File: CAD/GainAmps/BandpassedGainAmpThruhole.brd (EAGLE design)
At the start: 7.4 x 22.4 mm, 9 parts, among them U1 OPA202IDGKR

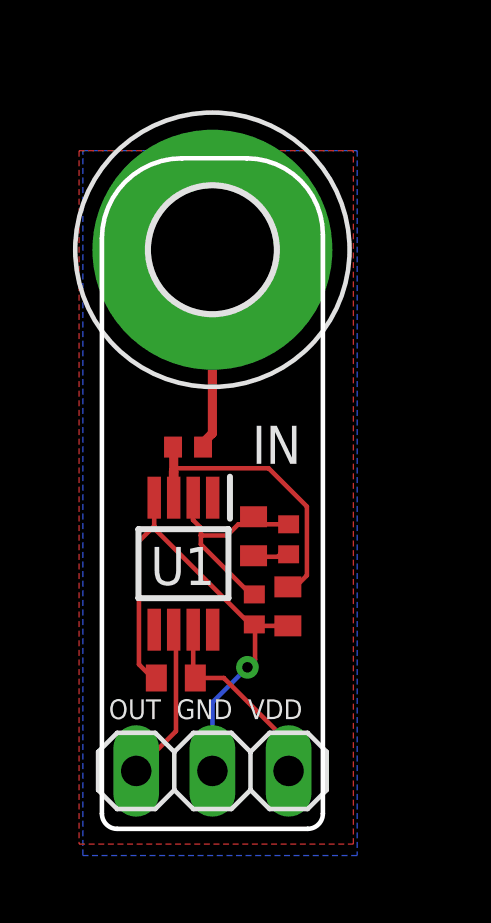
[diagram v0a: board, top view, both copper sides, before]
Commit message: moved, added production files for gain amps
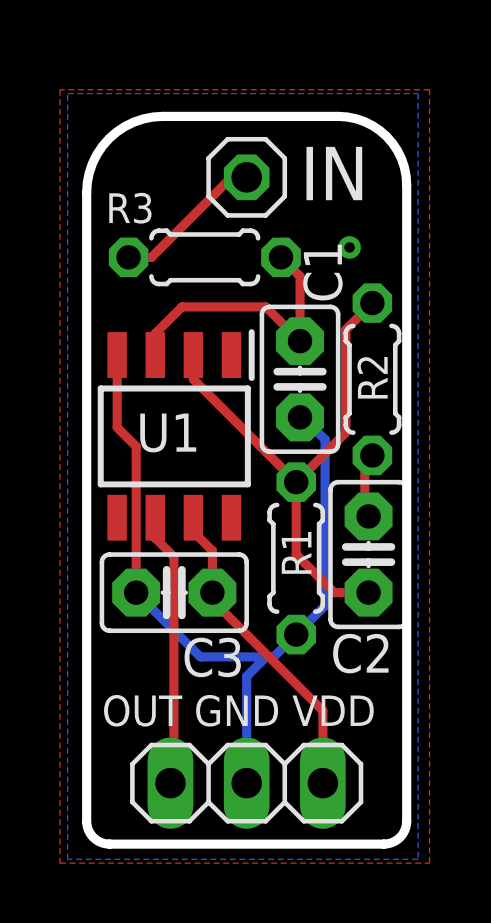
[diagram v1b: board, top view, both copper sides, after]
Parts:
- removed H1: MOUNT-PAD-ROUND4.1, holes:4,1-PAD
- added IN: (no value), pinhead:1X01
- C1, C2, C3: device rcl:C0402 -> capacitor-wima:C2.5-2
- R1, R2, R3: device rcl:R0402 -> rcl:0204/5
- U1: value OPA202IDGKR -> OPA202IDR; device OPA202IDGKR:SOP65P490X110-8N -> OPA202IDR:SOIC127P600X175-8N
- moved C1 7.58 mm to (8.13, 16.6)
- moved R3 6.35 mm to (4.95, 20.7), turned to 0 degrees
- moved R2 6.02 mm to (10.5, 16.6)
- moved U1 4.25 mm to (3.94, 14.7)
- moved C2 3.88 mm to (10.4, 10.8), turned to 90 degrees
- moved C3 2.85 mm to (3.94, 9.53), turned to 180 degrees
- moved R1 2.20 mm to (8.00, 10.7)
- moved JP1 1.21 mm to (6.35, 3.17)
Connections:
- net GND: now also C3.2; no longer C3.1
- net IN: now also IN.1; no longer H1.B4,1
- net VDD: now also C3.1; no longer C3.2
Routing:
- net -IN: track 8.01 -> 18.0 mm
- net GND: track 18.0 -> 27.2 mm
- net VDD: track 6.58 -> 10.6 mm
- net OUT: track 5.29 -> 9.18 mm
- net +IN: track 11.7 -> 9.44 mm
- net IN: track 6.71 -> 5.04 mm
- net N$3: track 1.47 -> 2.19 mm
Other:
- board size 7.4 x 22.4 mm -> 10.7 x 24.3 mm

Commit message: fixed edge plating
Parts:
- removed IN: (no value), pinhead:1X01
- added PAD1: (no value), wirepad:3,17/1,1
- moved R3 0.24 mm to (5.03, 20.5)
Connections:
- net IN: now also PAD1.1; no longer IN.1
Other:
- board size 10.7 x 24.3 mm -> 10.7 x 22.8 mm
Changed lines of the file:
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@@
 <setting verticaltext="up"/>
 </settings>
-<grid distance="1" unitdist="mil" unit="mil" style="lines" multiple="1" display="no" altdistance="5" altunitdist="mil" altunit="mil"/>
+<grid distance="10" unitdist="mil" unit="mil" style="lines" multiple="1" display="no" altdistance="5" altunitdist="mil" altunit="mil"/>
 <layers>
 <layer number="1" name="Top" color="4" fill="1" visible="yes" active="yes"/>
@@
 <board>
 <plain>
-<wire x1="10.922" y1="1.143" x2="1.778" y2="1.143" width="0.3048" layer="20"/>
-<wire x1="1.778" y1="1.143" x2="1.016" y2="1.905" width="0.3048" layer="20" curve="-90"/>
-<wire x1="1.016" y1="1.905" x2="1.016" y2="22.86" width="0.3048" layer="20"/>
-<wire x1="1.016" y1="22.86" x2="3.556" y2="25.4" width="0.3048" layer="20" curve="-90"/>
-<wire x1="3.556" y1="25.4" x2="9.398" y2="25.4" width="0.3048" layer="20"/>
-<wire x1="9.398" y1="25.4" x2="11.684" y2="23.114" width="0.3048" layer="20" curve="-90"/>
-<wire x1="11.684" y1="23.114" x2="11.684" y2="1.905" width="0.3048" layer="20"/>
-<wire x1="11.684" y1="1.905" x2="10.922" y2="1.143" width="0.3048" layer="20" curve="-90"/>
+<wire x1="10.922" y1="2.1336" x2="1.778" y2="2.1336" width="0.3048" layer="20"/>
+<wire x1="1.778" y1="2.1336" x2="1.016" y2="2.8956" width="0.3048" layer="20" curve="-90"/>
+<wire x1="1.016" y1="2.8956" x2="1.016" y2="22.352" width="0.3048" layer="20"/>
+<wire x1="1.016" y1="22.352" x2="3.556" y2="24.892" width="0.3048" layer="20" curve="-90"/>
+<wire x1="3.556" y1="24.892" x2="9.398" y2="24.892" width="0.3048" layer="20"/>
+<wire x1="9.398" y1="24.892" x2="11.684" y2="22.606" width="0.3048" layer="20" curve="-90"/>
+<wire x1="11.684" y1="22.606" x2="11.684" y2="2.8956" width="0.3048" layer="20"/>
+<wire x1="11.684" y1="2.8956" x2="10.922" y2="2.1336" width="0.3048" layer="20" curve="-90"/>
 <text x="8.128" y="22.606" size="1.778" layer="25">IN</text>
 <text x="1.524" y="5.08" size="1.016" layer="25">OUT GND VDD</text>
@@
 <attribute name="VALUE" x="8.2296" y="18.7706" size="0.9906" layer="27" ratio="10" rot="R270"/>
 </element>
-<element name="R3" library="rcl" library_urn="urn:adsk.eagle:library:334" package="0204/5" package3d_urn="urn:adsk.eagle:package:23488/1" value="1K" x="4.953" y="20.701" smashed="yes">
-<attribute name="NAME" x="3.2766" y="22.8346" size="0.9906" layer="25" ratio="10" rot="R180"/>
-<attribute name="POPULARITY" value="18" x="4.953" y="20.701" size="1.778" layer="27" display="off"/>
-<attribute name="SPICEPREFIX" value="R" x="4.953" y="20.701" size="1.778" layer="27" display="off"/>
-<attribute name="VALUE" x="4.0894" y="20.2946" size="0.9906" layer="27" ratio="10"/>
-</element>
-<element name="IN" library="pinhead" library_urn="urn:adsk.eagle:library:325" package="1X01" package3d_urn="urn:adsk.eagle:package:22485/2" value="" x="6.35" y="23.368" smashed="yes">
-<attribute name="POPULARITY" value="64" x="6.35" y="23.368" size="1.778" layer="27" display="off"/>
-<attribute name="VALUE" x="5.08" y="20.193" size="1.27" layer="27"/>
+<element name="R3" library="rcl" library_urn="urn:adsk.eagle:library:334" package="0204/5" package3d_urn="urn:adsk.eagle:package:23488/1" value="1K" x="5.0292" y="20.4724" smashed="yes">
+<attribute name="NAME" x="3.3528" y="22.606" size="0.9906" layer="25" ratio="10" rot="R180"/>
+<attribute name="POPULARITY" value="18" x="5.0292" y="20.4724" size="1.778" layer="27" display="off"/>
+<attribute name="SPICEPREFIX" value="R" x="5.0292" y="20.4724" size="1.778" layer="27" display="off"/>
+<attribute name="VALUE" x="4.1656" y="20.066" size="0.9906" layer="27" ratio="10"/>
 </element>
 <element name="JP1" library="pinhead" library_urn="urn:adsk.eagle:library:325" package="1X03" package3d_urn="urn:adsk.eagle:package:22458/2" value="" x="6.35" y="3.175" smashed="yes" rot="R180">
@@
 <attribute name="POPULARITY" value="28" x="3.937" y="9.525" size="1.778" layer="27" rot="R180" display="off"/>
 <attribute name="VALUE" x="5.588" y="12.319" size="1.27" layer="27" ratio="10" rot="R180"/>
+</element>
+<element name="PAD1" library="wirepad" library_urn="urn:adsk.eagle:library:412" package="3,17/1,1" package3d_urn="urn:adsk.eagle:package:30832/1" value="" x="6.1976" y="23.8252" smashed="yes">
+<attribute name="POPULARITY" value="3" x="6.1976" y="23.8252" size="1.778" layer="27" display="off"/>
+<attribute name="VALUE" x="6.1976" y="25.0252" size="0.0254" layer="27"/>
 </element>
 </elements>
@@
 <wire x1="6.35" y1="6.731" x2="6.35" y2="3.175" width="0.3048" layer="16"/>
 <polygon width="0.3048" layer="1">
-<vertex x="0.127" y="0.508"/>
-<vertex x="12.446" y="0.508"/>
-<vertex x="12.446" y="26.289"/>
-<vertex x="0.127" y="26.289"/>
+<vertex x="0.127" y="1.4986"/>
+<vertex x="12.446" y="1.4986"/>
+<vertex x="12.446" y="27.2796"/>
+<vertex x="0.127" y="27.2796"/>
 </polygon>
 <polygon width="0.3048" layer="16">
-<vertex x="0.381" y="0.635"/>
-<vertex x="0.381" y="26.162"/>
-<vertex x="12.065" y="26.162"/>
-<vertex x="12.065" y="0.635"/>
+<vertex x="0.381" y="1.6256"/>
+<vertex x="0.381" y="27.1526"/>
+<vertex x="12.065" y="27.1526"/>
+<vertex x="12.065" y="1.6256"/>
 </polygon>
 <via x="9.779" y="21.0312" extent="1-16" drill="0.35"/>
@@
 <contactref element="C1" pad="2"/>
 <contactref element="U1" pad="3"/>
-<wire x1="7.493" y1="20.701" x2="8.128" y2="20.066" width="0.3048" layer="1"/>
-<wire x1="8.128" y1="20.066" x2="8.128" y2="17.907" width="0.3048" layer="1"/>
+<wire x1="7.5692" y1="20.4724" x2="8.128" y2="19.9136" width="0.3048" layer="1"/>
+<wire x1="8.128" y1="19.9136" x2="8.128" y2="17.907" width="0.3048" layer="1"/>
 <wire x1="8.128" y1="17.907" x2="6.985" y2="19.05" width="0.3048" layer="1"/>
 <wire x1="6.985" y1="19.05" x2="4.191" y2="19.05" width="0.3048" layer="1"/>
@@
 <signal name="IN">
 <contactref element="R3" pad="1"/>
-<contactref element="IN" pad="1"/>
-<wire x1="6.35" y1="23.368" x2="5.842" y2="23.368" width="0.3048" layer="1"/>
-<wire x1="5.842" y1="23.368" x2="3.175" y2="20.701" width="0.3048" layer="1"/>
-<wire x1="3.175" y1="20.701" x2="2.413" y2="20.701" width="0.3048" layer="1"/>
+<wire x1="2.9464" y1="20.4724" x2="2.4892" y2="20.4724" width="0.3048" layer="1"/>
+<contactref element="PAD1" pad="1"/>
+<wire x1="6.1976" y1="23.8252" x2="6.1976" y2="23.7236" width="0.3048" layer="1"/>
+<wire x1="6.1976" y1="23.7236" x2="2.9464" y2="20.4724" width="0.3048" layer="1"/>
 </signal>
 </signals>

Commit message: fixes
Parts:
- removed R3: 1K, rcl:0204/5
- added REF: (no value), pinhead:1X01
- moved R1 6.86 mm to (7.75, 17.5), turned to 270 degrees
- moved R2 6.48 mm to (7.75, 10.8)
- moved C1 1.85 mm to (9.91, 17.1), turned to 270 degrees
- moved C2 0.25 mm to (10.2, 10.8), turned to 270 degrees
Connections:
- removed net -IN: C2.1, R1.2, R2.1, U1.2
- removed net N$3: C2.2, R2.2
- new net +REF: REF.1, U1.2
- new net R1C1: C1.1, R1.2
- net +IN: now also C2.1, R2.1; no longer R3.2
- net GND: now also JP1.3; no longer C1.1, JP1.2, R1.1
- net IN: now also R1.1; no longer R3.1
- net OUT: now also C2.2, JP1.1, R2.2; no longer JP1.3
- net VDD: now also JP1.2; no longer JP1.1
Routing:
- net -IN: track 18.0 -> 0.00 mm
- net GND: track 27.2 -> 15.0 mm
- net OUT: track 9.18 -> 18.1 mm
- net R1C1: track 0.00 -> 4.32 mm
- net +REF: track 0.00 -> 4.12 mm
- net +IN: track 9.18 -> 13.2 mm
- net N$3: track 2.19 -> 0.00 mm
- net IN: track 5.16 -> 4.40 mm
- net VDD: track 10.6 -> 10.0 mm
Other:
- board text added: "GND VDD OUT"
- board text removed: "OUT GND VDD"
